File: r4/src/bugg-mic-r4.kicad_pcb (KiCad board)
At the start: 2 copper layers, 30.5 x 22 mm, 25 parts, among them J101 2842142-4, U101 PCMD3180

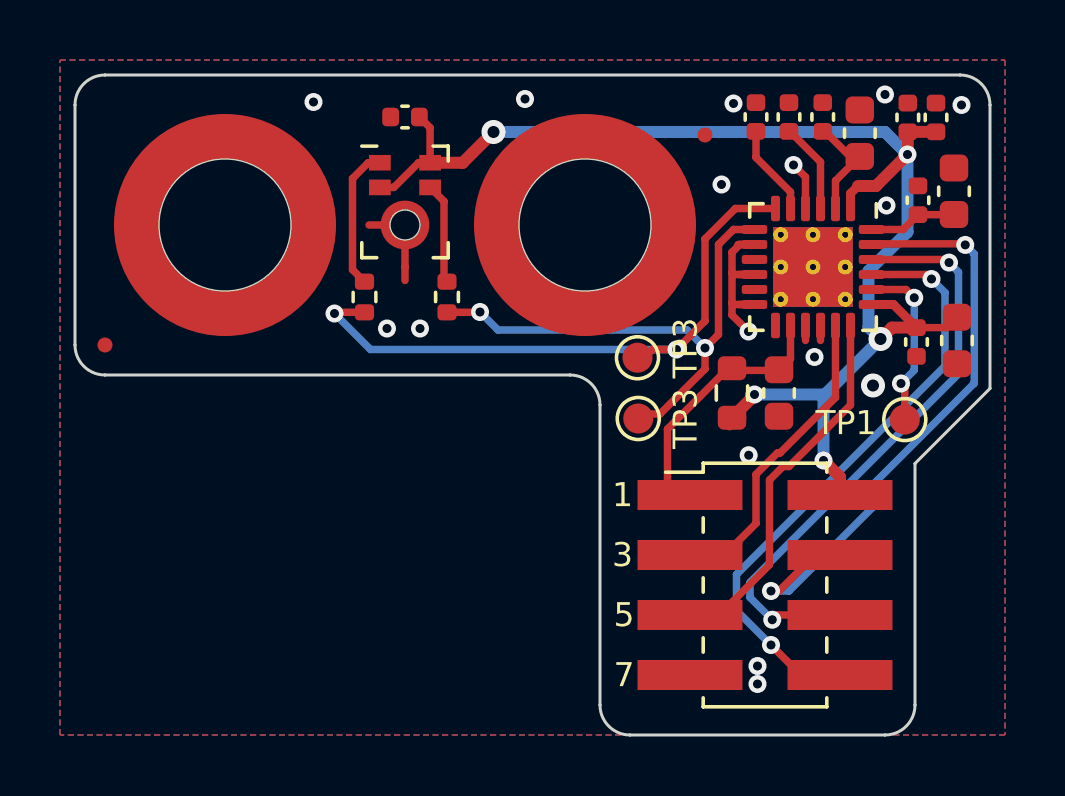
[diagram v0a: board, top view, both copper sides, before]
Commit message: Update Wurth spacers to remove DRC violations. DRC pass
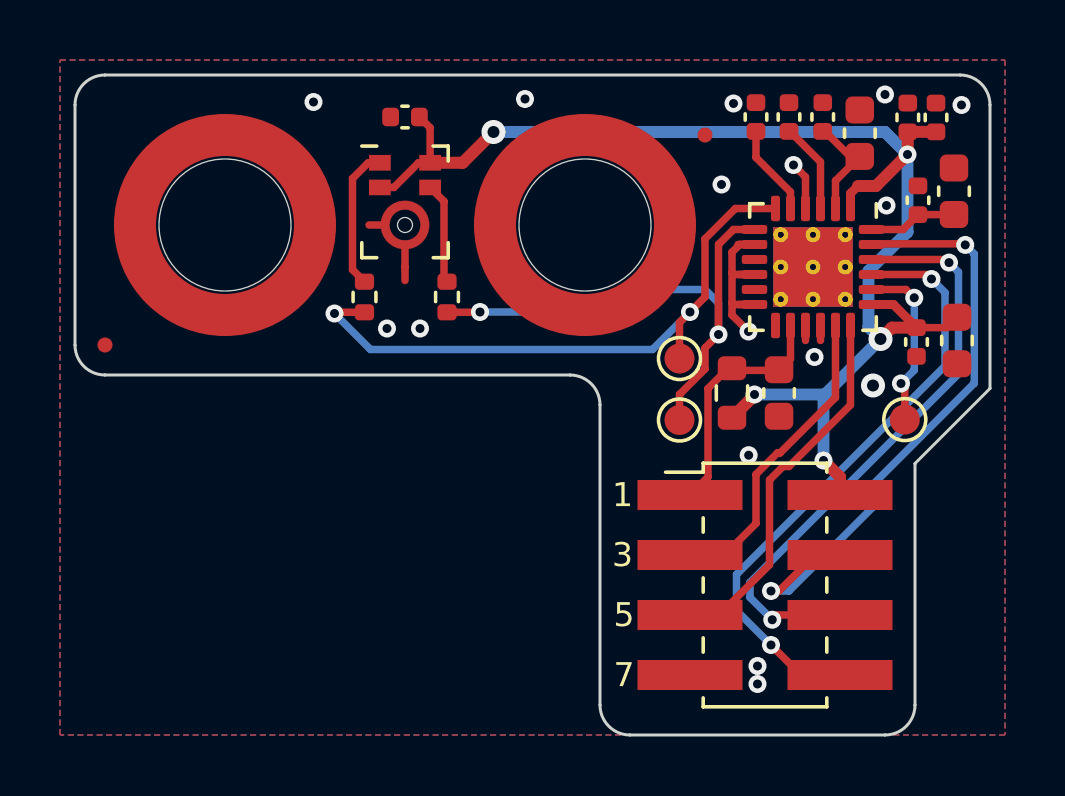
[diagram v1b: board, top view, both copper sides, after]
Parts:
- H301: renamed from H101; footprint Mounting_Wuerth:Mounting_Wuerth_WA-SMSI-M3_H7mm_9774070360 -> jeffmakes-footprints:Mounting_Wuerth_WA-SMSI-M3_H7mm_9774070360
- H302: renamed from H102; footprint Mounting_Wuerth:Mounting_Wuerth_WA-SMSI-M3_H7mm_9774070360 -> jeffmakes-footprints:Mounting_Wuerth_WA-SMSI-M3_H7mm_9774070360
- moved TP301 1.40 mm to (9.15, 4.45)
- moved TP302 1.38 mm to (9.15, 6.50)
- renumbered C101 to C301, C102 to C302, C103 to C303, C104 to C304, C105 to C305, C106 to C306, C107 to C307, C108 to C308, C109 to C309, C110 to C310, C111 to C311, C112 to C312, FID1 to FID301, FID2 to FID302, J101 to J301, MIC101 to MIC301, R101 to R301, R102 to R302, R103 to R303, TP102 to TP301, TP103 to TP302, TP101 to TP303, U101 to U301
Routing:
- net /SCL: track 11.1 -> 10.4 mm
- net Net-(U301-PDMCLK1_GPO1): track 17.7 -> 18.4 mm
- net +3V3: track 46.7 -> 46.1 mm
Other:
- board text added: "bugg-mic-r4"
- board text removed: "TP1"
- board text removed: "TP3"
- board text removed: "bugg-mic-r3"

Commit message: Silkscreen done. DRC pass
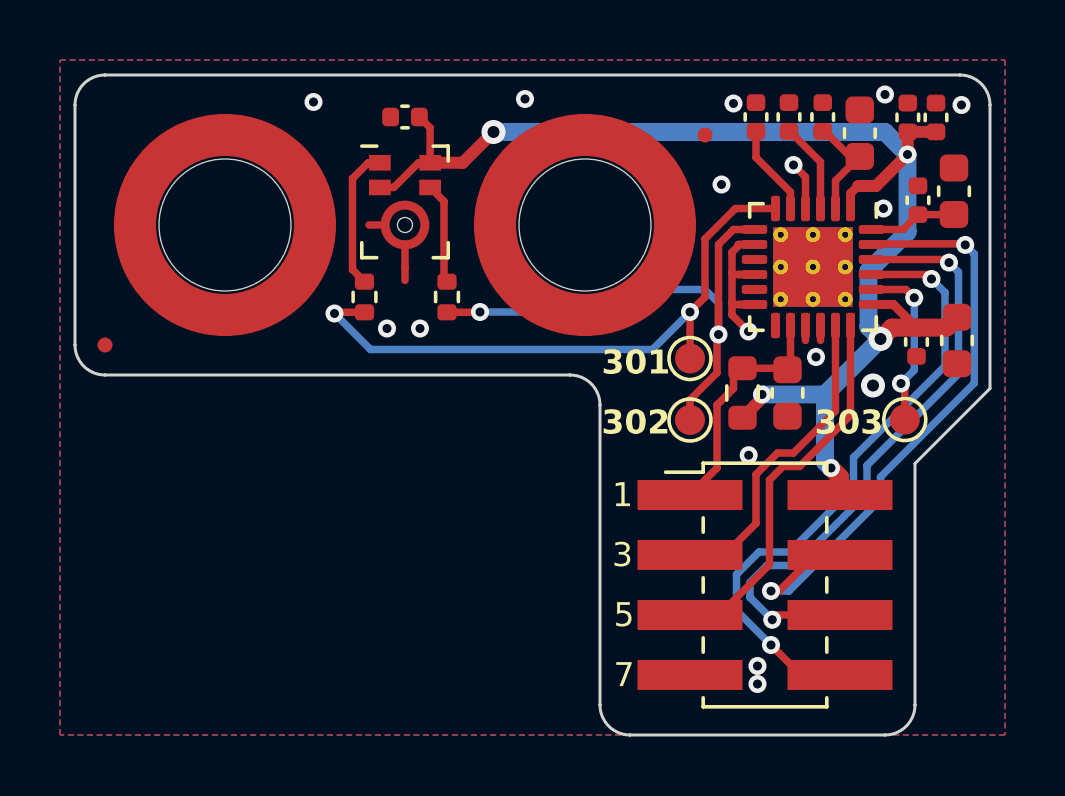
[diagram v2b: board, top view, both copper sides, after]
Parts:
- moved R303 0.35 mm to (11.2, 5.60)
- moved TP301 0.35 mm to (9.50, 4.45)
- moved TP302 0.35 mm to (9.50, 6.50)
- moved C312 0.28 mm to (12.8, 5.60)
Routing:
- net /SDOUT: track 20.5 -> 21.1 mm
- net /BCLK: track 20.2 -> 20.7 mm
- added copper zone on In1.Cu, net GND
- added copper zone on In2.Cu, net GND
- added copper zone on In3.Cu, net GND
- added copper zone on In4.Cu, net GND
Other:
- copper layers 2 -> 6
- board text added: "301"
- board text added: "302"
- board text added: "303"

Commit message: Add some cap voltages and other bom-related parameters
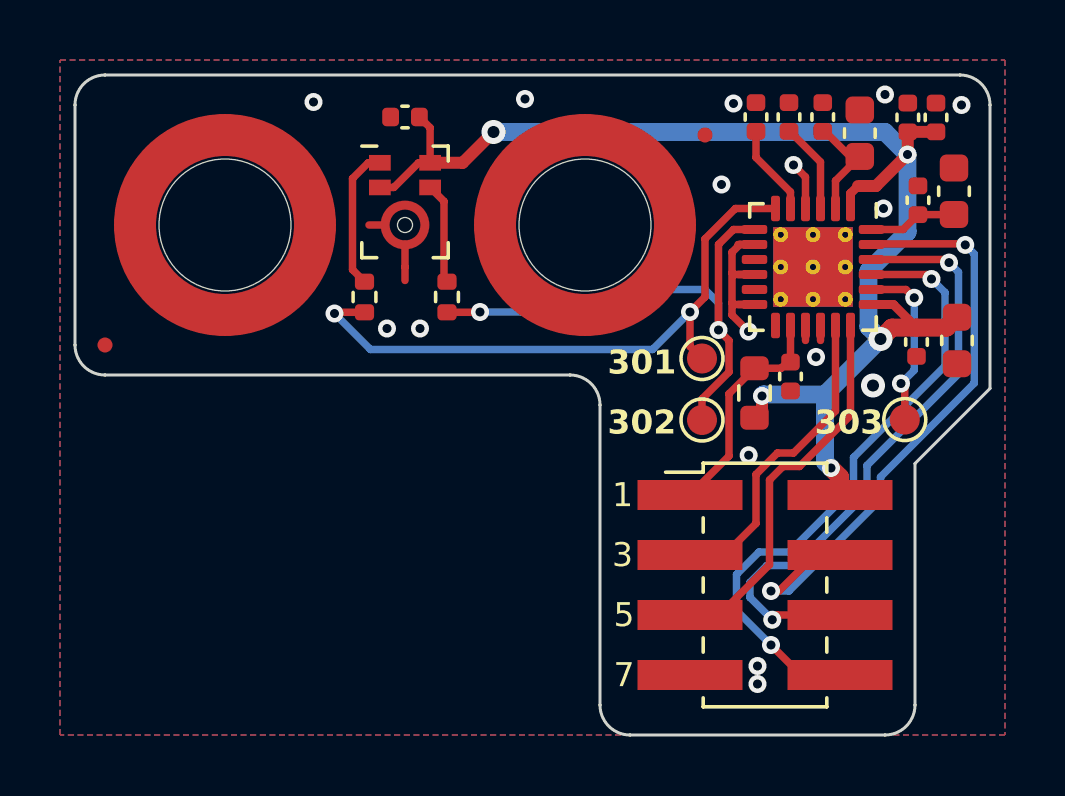
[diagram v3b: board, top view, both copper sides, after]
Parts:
- C312: footprint Capacitor_SMD:C_0603_1608Metric -> Capacitor_SMD:C_0402_1005Metric
- moved C312 0.56 mm to (12.8, 5.05)
- moved R303 0.40 mm to (11.7, 5.60)
- moved TP301 0.40 mm to (9.90, 4.45)
- moved TP302 0.40 mm to (9.90, 6.50)

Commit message: Fix central core thickness. DRC pass
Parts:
- R301, R302: value 22R -> 33R
- renumbered H301 to SP301, H302 to SP302
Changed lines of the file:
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@@
 (kicad_pcb (version 20221018) (generator pcbnew)
   (general
-    (thickness 1.49)
+    (thickness 1.6)
   )
   (paper "A4")
@@
       (layer "dielectric 2" (type "core") (thickness 0.3) (material "FR4") (epsilon_r 4.5) (loss_tangent 0.02))
       (layer "In2.Cu" (type "copper") (thickness 0.035))
-      (layer "dielectric 3" (type "prepreg") (thickness 0.22) (material "FR4") (epsilon_r 4.5) (loss_tangent 0.02))
+      (layer "dielectric 3" (type "prepreg") (thickness 0.33) (material "FR4") (epsilon_r 4.5) (loss_tangent 0.02))
       (layer "In3.Cu" (type "copper") (thickness 0.035))
       (layer "dielectric 4" (type "core") (thickness 0.3) (material "FR4") (epsilon_r 4.5) (loss_tangent 0.02))
@@
     (property "ki_keywords" "mounting hole")
     (attr smd)
-    (fp_text reference "H302" (at 0 -4.65) (layer "F.SilkS") hide
+    (fp_text reference "SP302" (at 0 -4.65) (layer "F.SilkS") hide
         (effects (font (size 1 1) (thickness 0.15)))
     )
@@
         (effects (font (size 1 1) (thickness 0.15)))
     )
-    (fp_text value "22R" (at 0 1.17 90) (layer "F.Fab")
+    (fp_text value "33R" (at 0 1.17 90) (layer "F.Fab")
         (effects (font (size 1 1) (thickness 0.15)))
     )
@@
         (effects (font (size 1 1) (thickness 0.15)))
     )
-    (fp_text value "22R" (at 0 1.17 90) (layer "F.Fab")
+    (fp_text value "33R" (at 0 1.17 90) (layer "F.Fab")
         (effects (font (size 1 1) (thickness 0.15)))
     )
@@
     (property "ki_keywords" "mounting hole")
     (attr smd)
-    (fp_text reference "H301" (at 0 -4.65) (layer "F.SilkS") hide
-        (effects (font (size 1 1) (thickness 0.15)))
-    )
+    (fp_text reference "SP301" (at 0 -4.65) (layer "F.SilkS") hide
+        (effects (font (size 1 1) (thickness 0.15)))
+    )
